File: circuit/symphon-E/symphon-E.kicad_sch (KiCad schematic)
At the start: 1 part

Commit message: add pinout
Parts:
- gave numbers to parts that had none: 1
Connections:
- net keypad_C1_3: now reaches U1.10 (D7)
- net keypad_C2_4: now reaches U1.11 (D8)
- net keypad_R4_6: now reaches U1.13 (~D10)
- net keypad_R3_7: now reaches U1.14 (~D11)
- net keypad_C3_8: now reaches U1.15 (D12)
- net AUDIO_OUT: now reaches U1.20 (A1/D15)
- net ENCODER_BTN: now reaches U1.22 (A3/D17)
- net DISPLAY_SDA: now reaches U1.23 (A4/D18)
- net DISPLAY_SCL: now reaches U1.24 (A5/D19)
- net ENCODER_A: now reaches U1.5 (D2)
- net ENCODER_B: now reaches U1.6 (~D3)
- net keypad_R1_1: now reaches U1.7 (D4)
- net keypad_R2_2: now reaches U1.8 (~D5)
- net RINGER_OUT: now reaches U1.9 (~D6)
- no-connect marks 0 -> 4
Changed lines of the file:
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@@
 (kicad_sch (version 20211123) (generator eeschema)
   (paper "A4")
+  (no_connect (at 69.85 44.45))
+  (no_connect (at 8.89 43.18))
+  (no_connect (at 69.85 67.31))
+  (no_connect (at 69.85 41.91))
+  (global_label "ENCODER_A" (shape input) (at 39.37 41.91 180) (fields_autoplaced)
+    (effects (font (size 1.27 1.27)) (justify right))
+    (property "Intersheet References" "${INTERSHEET_REFS}" (id 0) (at 26.1317 41.8306 0)
+      (effects (font (size 1.27 1.27)) (justify right) hide)
+    )
+  )
+  (global_label "keypad_R2_2" (shape input) (at 39.37 49.53 180) (fields_autoplaced)
+    (effects (font (size 1.27 1.27)) (justify right))
+    (property "Intersheet References" "${INTERSHEET_REFS}" (id 0) (at 24.8012 49.4506 0)
+      (effects (font (size 1.27 1.27)) (justify right) hide)
+    )
+  )
+  (global_label "keypad_R4_6" (shape input) (at 39.37 62.23 180) (fields_autoplaced)
+    (effects (font (size 1.27 1.27)) (justify right))
+    (property "Intersheet References" "${INTERSHEET_REFS}" (id 0) (at 24.8012 62.1506 0)
+      (effects (font (size 1.27 1.27)) (justify right) hide)
+    )
+  )
+  (global_label "keypad_C2_4" (shape input) (at 39.37 57.15 180) (fields_autoplaced)
+    (effects (font (size 1.27 1.27)) (justify right))
+    (property "Intersheet References" "${INTERSHEET_REFS}" (id 0) (at 24.8012 57.0706 0)
+      (effects (font (size 1.27 1.27)) (justify right) hide)
+    )
+  )
+  (global_label "DISPLAY_SCL" (shape input) (at 69.85 46.99 0) (fields_autoplaced)
+    (effects (font (size 1.27 1.27)) (justify left))
+    (property "Intersheet References" "${INTERSHEET_REFS}" (id 0) (at 84.2979 46.9106 0)
+      (effects (font (size 1.27 1.27)) (justify left) hide)
+    )
+  )
+  (global_label "DISPLAY_SDA" (shape input) (at 69.85 49.53 0) (fields_autoplaced)
+    (effects (font (size 1.27 1.27)) (justify left))
+    (property "Intersheet References" "${INTERSHEET_REFS}" (id 0) (at 84.3583 49.4506 0)
+      (effects (font (size 1.27 1.27)) (justify left) hide)
+    )
+  )
+  (global_label "keypad_R1_1" (shape input) (at 39.37 46.99 180) (fields_autoplaced)
+    (effects (font (size 1.27 1.27)) (justify right))
+    (property "Intersheet References" "${INTERSHEET_REFS}" (id 0) (at 24.8012 46.9106 0)
+      (effects (font (size 1.27 1.27)) (justify right) hide)
+    )
+  )
+  (global_label "RINGER_OUT" (shape input) (at 39.37 52.07 180) (fields_autoplaced)
+    (effects (font (size 1.27 1.27)) (justify right))
+    (property "Intersheet References" "${INTERSHEET_REFS}" (id 0) (at 25.4664 51.9906 0)
+      (effects (font (size 1.27 1.27)) (justify right) hide)
+    )
+  )
+  (global_label "keypad_C1_3" (shape input) (at 39.37 54.61 180) (fields_autoplaced)
+    (effects (font (size 1.27 1.27)) (justify right))
+    (property "Intersheet References" "${INTERSHEET_REFS}" (id 0) (at 24.8012 54.5306 0)
+      (effects (font (size 1.27 1.27)) (justify right) hide)
+    )
+  )
+  (global_label "AUDIO_OUT" (shape input) (at 69.85 57.15 0) (fields_autoplaced)
+    (effects (font (size 1.27 1.27)) (justify left))
+    (property "Intersheet References" "${INTERSHEET_REFS}" (id 0) (at 82.4836 57.0706 0)
+      (effects (font (size 1.27 1.27)) (justify left) hide)
+    )
+  )
+  (global_label "ENCODER_B" (shape input) (at 39.37 44.45 180) (fields_autoplaced)
+    (effects (font (size 1.27 1.27)) (justify right))
+    (property "Intersheet References" "${INTERSHEET_REFS}" (id 0) (at 25.9502 44.3706 0)
+      (effects (font (size 1.27 1.27)) (justify right) hide)
+    )
+  )
+  (global_label "ENCODER_BTN" (shape input) (at 69.85 52.07 0) (fields_autoplaced)
+    (effects (font (size 1.27 1.27)) (justify left))
+    (property "Intersheet References" "${INTERSHEET_REFS}" (id 0) (at 85.5679 51.9906 0)
+      (effects (font (size 1.27 1.27)) (justify left) hide)
+    )
+  )
+  (global_label "keypad_R3_7" (shape input) (at 39.37 64.77 180) (fields_autoplaced)
+    (effects (font (size 1.27 1.27)) (justify right))
+    (property "Intersheet References" "${INTERSHEET_REFS}" (id 0) (at 24.8012 64.6906 0)
+      (effects (font (size 1.27 1.27)) (justify right) hide)
+    )
+  )
+  (global_label "keypad_C3_8" (shape input) (at 39.37 67.31 180) (fields_autoplaced)
+    (effects (font (size 1.27 1.27)) (justify right))
+    (property "Intersheet References" "${INTERSHEET_REFS}" (id 0) (at 24.8012 67.2306 0)
+      (effects (font (size 1.27 1.27)) (justify right) hide)
+    )
+  )
   (symbol (lib_id "Arduino:Arduino_Nano") (at 54.61 49.53 0) (unit 1)
     (in_bom yes) (on_board yes) (fields_autoplaced)
-    (property "Reference" "U?" (id 0) (at 54.61 24.13 0))
+    (property "Reference" "U1" (id 0) (at 54.61 24.13 0))
     (property "Value" "Arduino_Nano" (id 1) (at 54.61 26.67 0))
     (property "Footprint" "Arduino:Arduino_Nano" (id 2) (at 54.61 71.12 0)
@@
   (symbol_instances
     (path "/05df8035-1ae4-4fd6-8683-6c4f92e2cd4b"
-      (reference "U?") (unit 1) (value "Arduino_Nano") (footprint "Arduino:Arduino_Nano")
+      (reference "U1") (unit 1) (value "Arduino_Nano") (footprint "Arduino:Arduino_Nano")
     )
   )

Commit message: add pcb
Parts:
- added J1: display_headers, Connector_JST:JST_EH_B4B-EH-A_1x04_P2.50mm_Vertical, symbol Connector:Conn_01x04_Male
- added J10: Potentiometer, Connector_JST:JST_EH_B3B-EH-A_1x03_P2.50mm_Vertical, symbol Connector:Conn_01x03_Male
- added J2, J3: power_in, Connector_JST:JST_EH_B2B-EH-A_1x02_P2.50mm_Vertical, symbol Connector:Conn_01x02_Male
- added J4: RINGER_HEADER, Connector_JST:JST_EH_B2B-EH-A_1x02_P2.50mm_Vertical, symbol Connector:Conn_01x02_Male
- added J5: ENCODER_HEADER, Connector_JST:JST_EH_B5B-EH-A_1x05_P2.50mm_Vertical, symbol Connector:Conn_01x05_Male
- added J6: KEYPAD_HEADER, Connector_JST:JST_EH_B8B-EH-A_1x08_P2.50mm_Vertical, symbol Connector:Conn_01x08_Male
- added J7: MIC_HEADER, Connector_JST:JST_EH_B2B-EH-A_1x02_P2.50mm_Vertical, symbol Connector:Conn_01x02_Male
- added J8: 9MM_HEADER, Connector_JST:JST_EH_B2B-EH-A_1x02_P2.50mm_Vertical, symbol Connector:Conn_01x02_Male
- added J9: AUDIO_HEADER, Connector_JST:JST_EH_B2B-EH-A_1x02_P2.50mm_Vertical, symbol Connector:Conn_01x02_Male
- added Q1: IRLB8721PBF, Package_TO_SOT_THT:TO-220-3_Vertical, symbol Transistor_FET:IRLB8721PBF
- added R1: 1k, Resistor_THT:R_Axial_DIN0204_L3.6mm_D1.6mm_P7.62mm_Horizontal, symbol Device:R_Small_US
- added R2: 1k, Resistor_THT:R_Axial_DIN0204_L3.6mm_D1.6mm_P7.62mm_Horizontal, symbol Device:R_US
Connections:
- net AUDIO_OUT: now also J8.2 (Pin_2), J9.1 (Pin_1), R1.2, R2.1; no longer U1.20 (A1/D15)
- net DISPLAY_SCL: now also J1.2 (Pin_2)
- net DISPLAY_SDA: now also J1.1 (Pin_1)
- net ENCODER_A: now also J5.2 (Pin_2)
- net ENCODER_B: now also J5.1 (Pin_1)
- net ENCODER_BTN: now also J5.3 (Pin_3)
- net RINGER_OUT: now also Q1.1 (G)
- net keypad_C1_3: now also J6.6 (Pin_6)
- net keypad_C2_4: now also J6.5 (Pin_5)
- net keypad_C3_8: now also J6.1 (Pin_1)
- net keypad_R1_1: now also J6.8 (Pin_8)
- net keypad_R2_2: now also J6.7 (Pin_7)
- net keypad_R3_7: now also J6.2 (Pin_2)
- net keypad_R4_6: now also J6.3 (Pin_3)
- net keypad_XX_5: now reaches U1.12 (~D9)
- net keypad_XX_5: now also J6.4 (Pin_4)
- net 5V: now reaches U1.27 (+5V)
- net 5V: now also J1.3 (Pin_3), J2.2 (Pin_2), J5.4 (Pin_4)
- net GND: now reaches U1.29 (GND)
- net GND: now also U1.4 (GND), J1.4 (Pin_4), J10.3 (Pin_3), J2.1 (Pin_1), J3.1 (Pin_1), J4.2 (Pin_2), J5.5 (Pin_5), J7.2 (Pin_2), J8.1 (Pin_1), J9.2 (Pin_2)
- net VCC: now reaches U1.30 (VIN)
- new net: R1.1, U1.20 (A1/D15)
- new net 12V: J3.2 (Pin_2), Q1.3 (S)
- new net AMP_IN: J10.2 (Pin_2)
- new net DRAIN: J4.1 (Pin_1), Q1.2 (D)
- new net MIC_OUT_2: J10.1 (Pin_1), J7.1 (Pin_1), R2.2
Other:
- note added: "12v power in"
- note added: "5v power in"
- note added: "9mm Jack"
- note added: "Arduino"
- note added: "Audio out"
- note added: "Dislpay"
- note added: "Encoder"
- note added: "Keypad"
- note added: "Ringer"
- note added: "Volume"
- moved on the sheet: U1

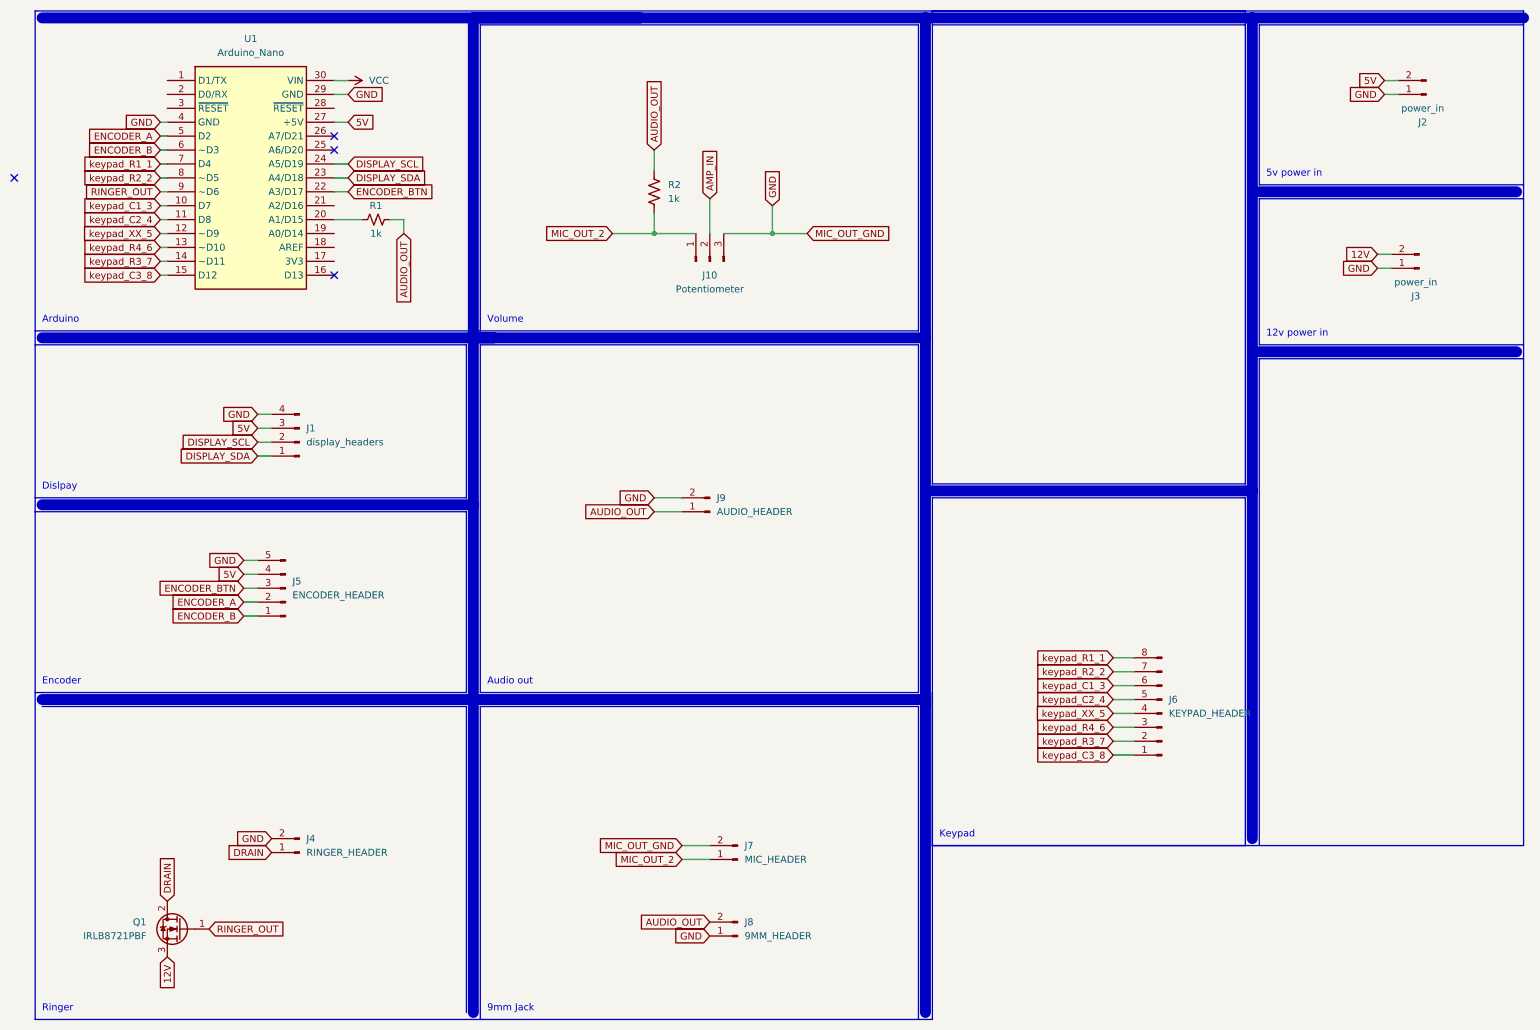
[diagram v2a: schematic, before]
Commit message: update schematic
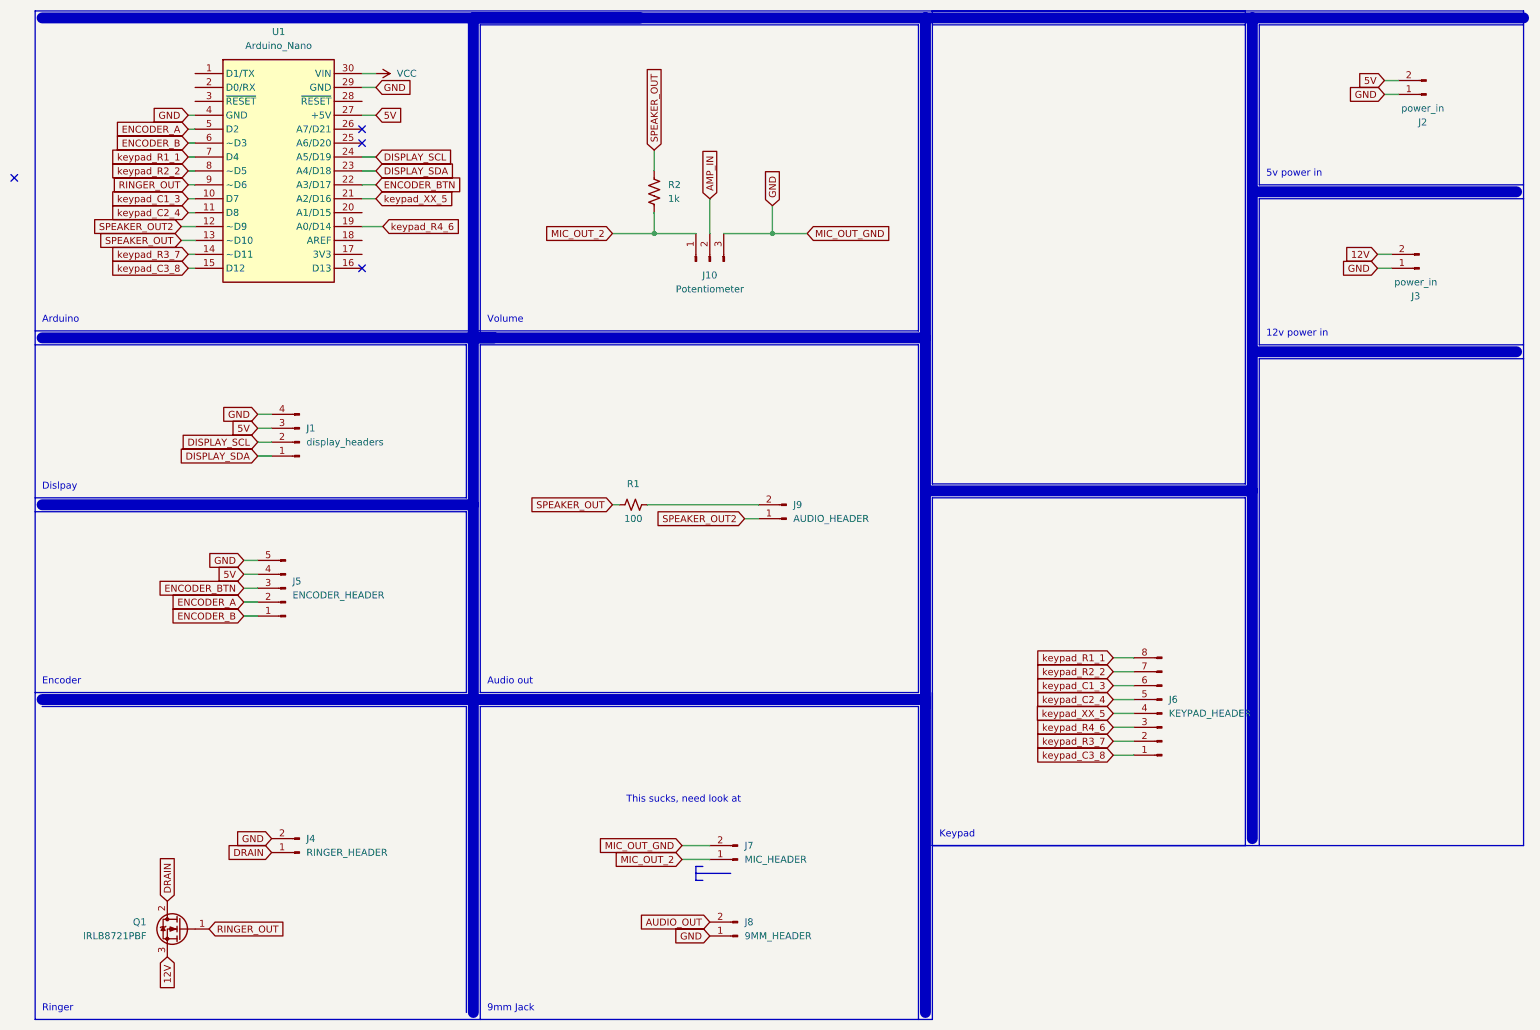
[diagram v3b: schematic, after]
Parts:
- R1: value 1k -> 100
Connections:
- net AUDIO_OUT: no longer J9.1 (Pin_1), R1.2, R2.1
- net GND: no longer J9.2 (Pin_2)
- net keypad_R4_6: now also U1.19 (A0/D14); no longer U1.13 (~D10)
- net keypad_XX_5: now also U1.21 (A2/D16); no longer U1.12 (~D9)
- net at U1.20 (A1/D15): no longer R1.1
- new net: J9.2 (Pin_2), R1.2
- new net SPEAKER_OUT: R1.1, R2.1, U1.13 (~D10)
- new net SPEAKER_OUT2: J9.1 (Pin_1), U1.12 (~D9)
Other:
- note added: "This sucks, need look at"
- moved on the sheet: J9, U1
